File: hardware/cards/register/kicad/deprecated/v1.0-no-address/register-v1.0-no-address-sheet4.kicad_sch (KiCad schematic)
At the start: 8 parts, among them IC10 74*32, IC24 74*32, IC25 74*192, IC26 74*192, IC27 74*192, IC28 74*192, IC29 74*244, IC30 74*244

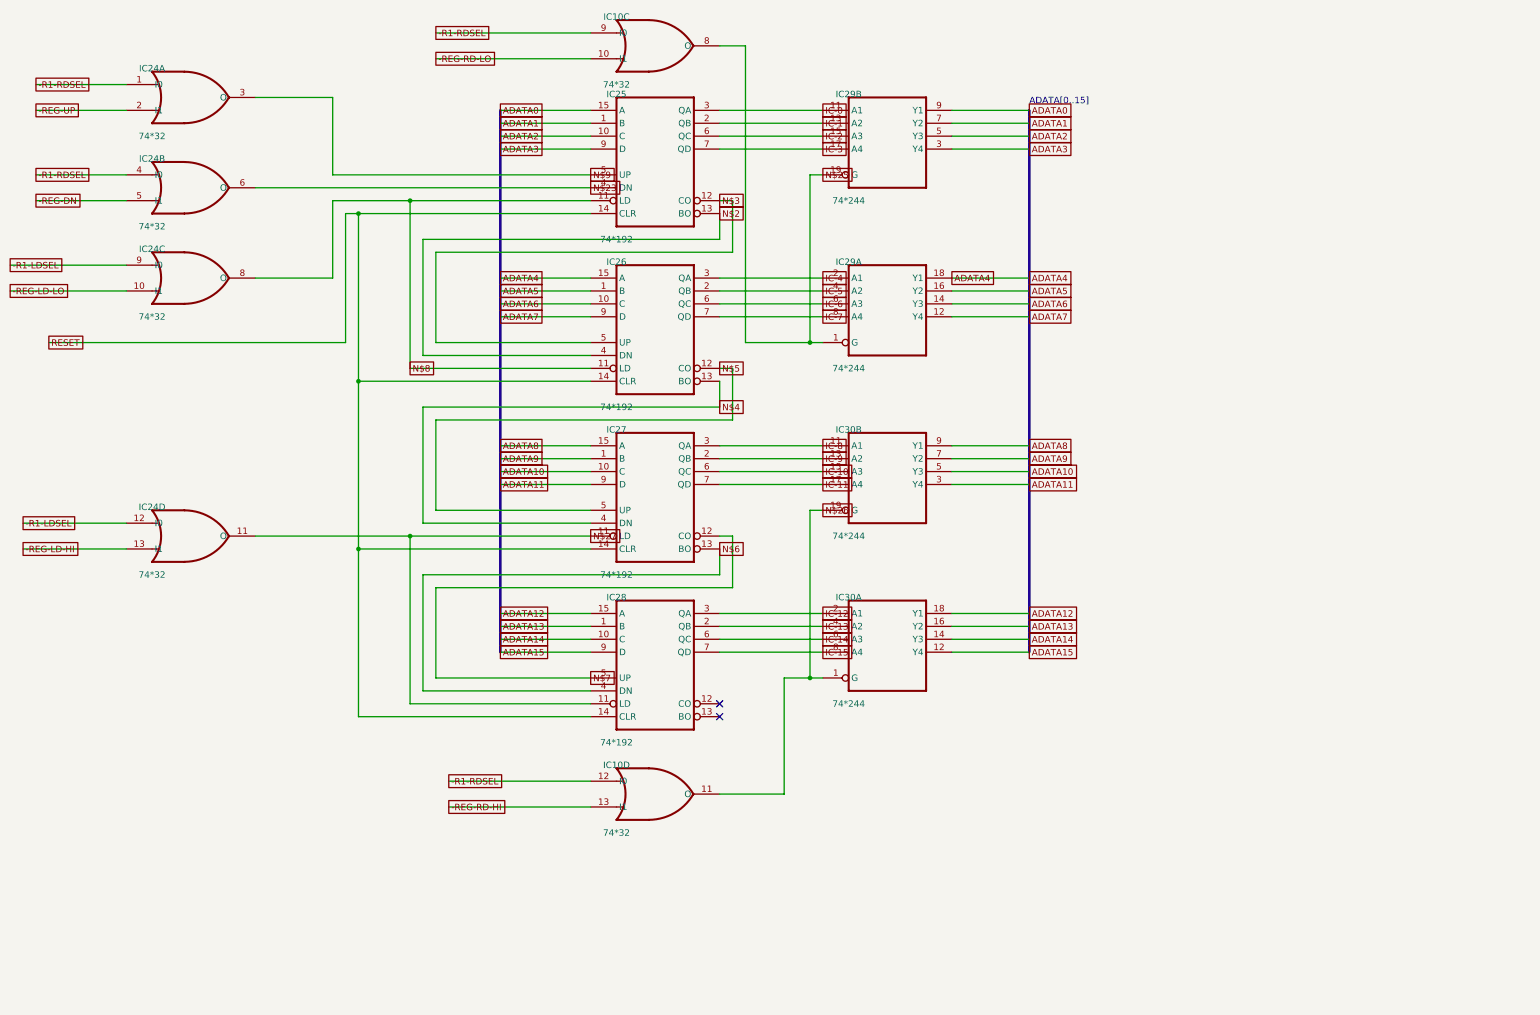
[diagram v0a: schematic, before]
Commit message: fix(kicad): readable converted schematics - overlaps 42,847 -> 3,147, nothing off the frame; CF sheet 0 overlaps
- tools/kicad/sch_overlaps.py: calibrated readability check (text/text, text/body, text/line, off frame/title block)
- eagle_sch_to_kicad.py: fields placed from Eagle's smashed attributes or the symbol's >NAME/>VALUE with Eagle's align,
  size and ratio, readable angles; fields Eagle never shows hidden (FABC96R shows only its pin name); pin numbers hidden
  where every Eagle pin hides them; Eagle-hidden layers dropped (the stray SpiceOrder text); labels on their own wires,
  converter labels only where KiCad needs them; rotate-then-mirror fixed for MR90/MR270 in pin_world/no-connects;
  each sheet on the smallest page that holds it, centred clear of the title block
- finish_board.py: stable footprint-library choice (DRC counts no longer vary run to run)
- all 37 projects regenerated: netlist proofs unchanged (34 MATCH, 2 schematic-only, video Fusion export MISMATCH as
  before); DRC same or better; ERC up (loose wire ends onto graphic buses no longer hidden by labels; explained per README)
- CF card: gate names off the gate bodies, U3 clear of its title, 5.08 mm connector pins; rebuilt: DRC 0/0, proof MATCH
- schematic PDFs regenerated (tools/sch_to_pdf.py, 37/37)

Co-Authored-By: Claude Opus 5.5 <noreply@anthropic.com>
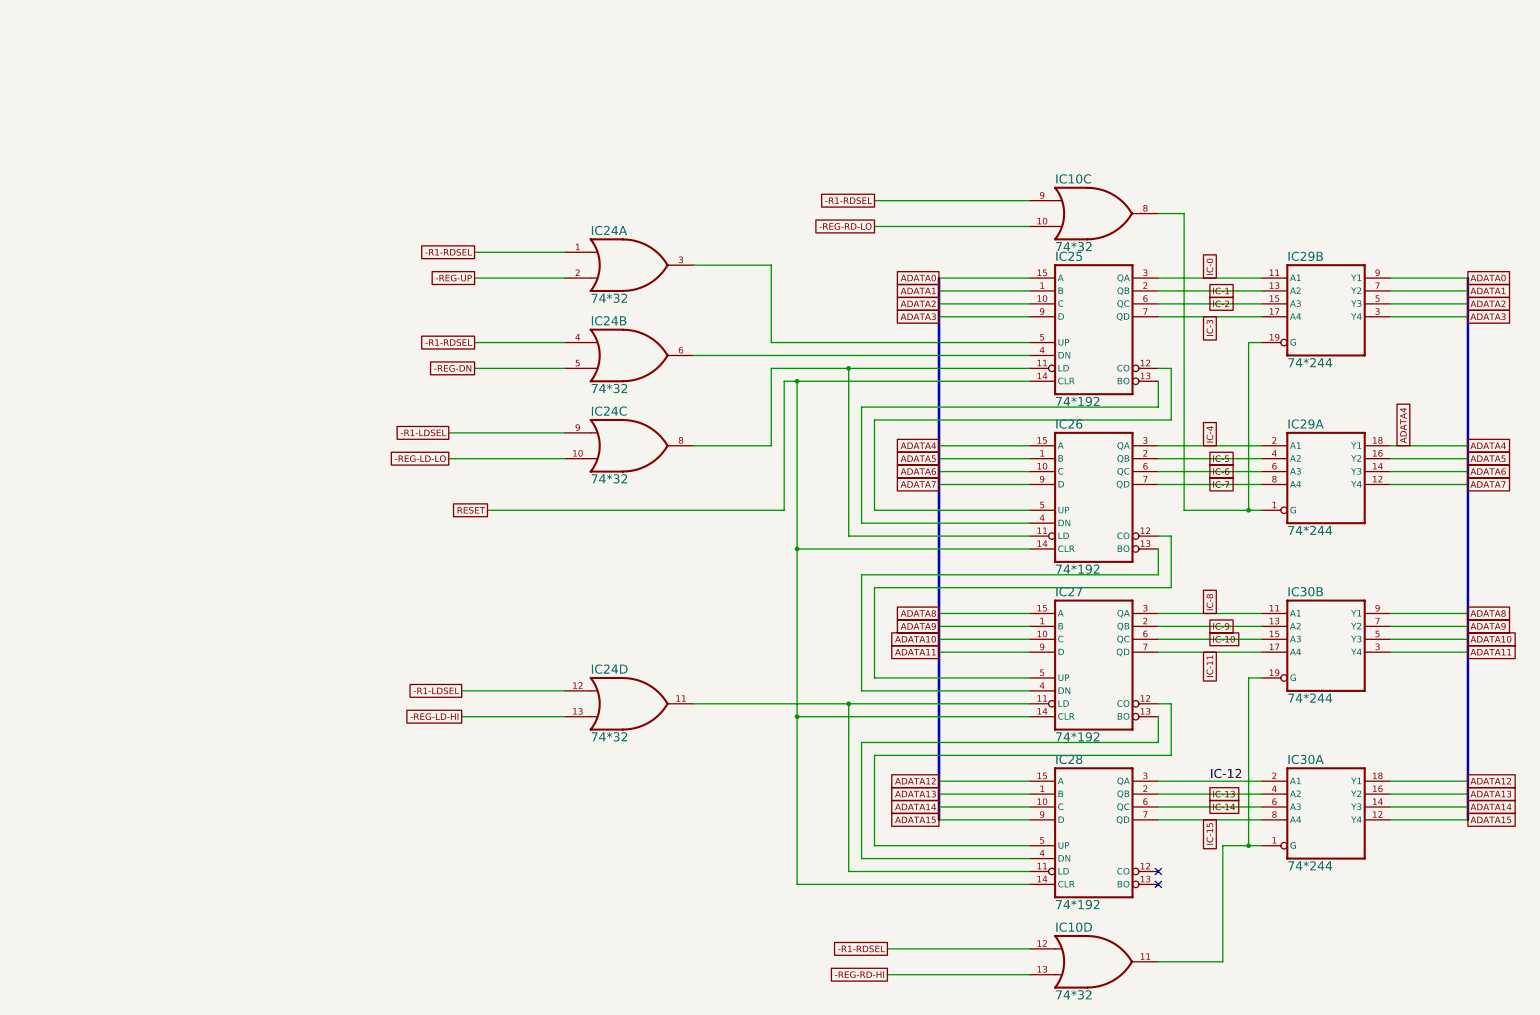
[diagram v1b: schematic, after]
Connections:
- net N$2: no longer names the net of IC25.13 (BO), IC26.4 (DN)
- net N$23: no longer names the net of IC24.6 (O), IC25.4 (DN)
- net N$25: no longer names the net of IC10.8 (O), IC29.1 (G), IC29.19 (G)
- net N$26: no longer names the net of IC10.11 (O), IC30.1 (G), IC30.19 (G)
- net N$27: no longer names the net of IC24.11 (O), IC27.11 (LD), IC28.11 (LD)
- net N$3: no longer names the net of IC25.12 (CO), IC26.5 (UP)
- net N$4: no longer names the net of IC26.13 (BO), IC27.4 (DN)
- net N$5: no longer names the net of IC26.12 (CO), IC27.5 (UP)
- net N$6: no longer names the net of IC27.13 (BO), IC28.4 (DN)
- net N$7: no longer names the net of IC27.12 (CO), IC28.5 (UP)
- net N$8: no longer names the net of IC24.8 (O), IC25.11 (LD), IC26.11 (LD)
- net N$9: no longer names the net of IC24.3 (O), IC25.5 (UP)
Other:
- note removed: "ADATA[0..15]"
- moved on the sheet: IC25, IC26, IC27, IC28, IC29A, IC29B, IC30A, IC30B
